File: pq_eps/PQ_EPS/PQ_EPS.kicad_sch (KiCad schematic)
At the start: 89 parts, among them IC1 DS2782E+, IC2 ISL9120IRTNZ, J1 CES-110-02-L-S, J2 CES-110-02-L-S, J3 CES-110-02-L-S, J4 CES-110-02-L-S, Q1 SIR424DP, U1 SPV1040TTR, U2 SPV1040TTR, U3 SPV1040TTR, U4 LTC4040EUFD#PBF

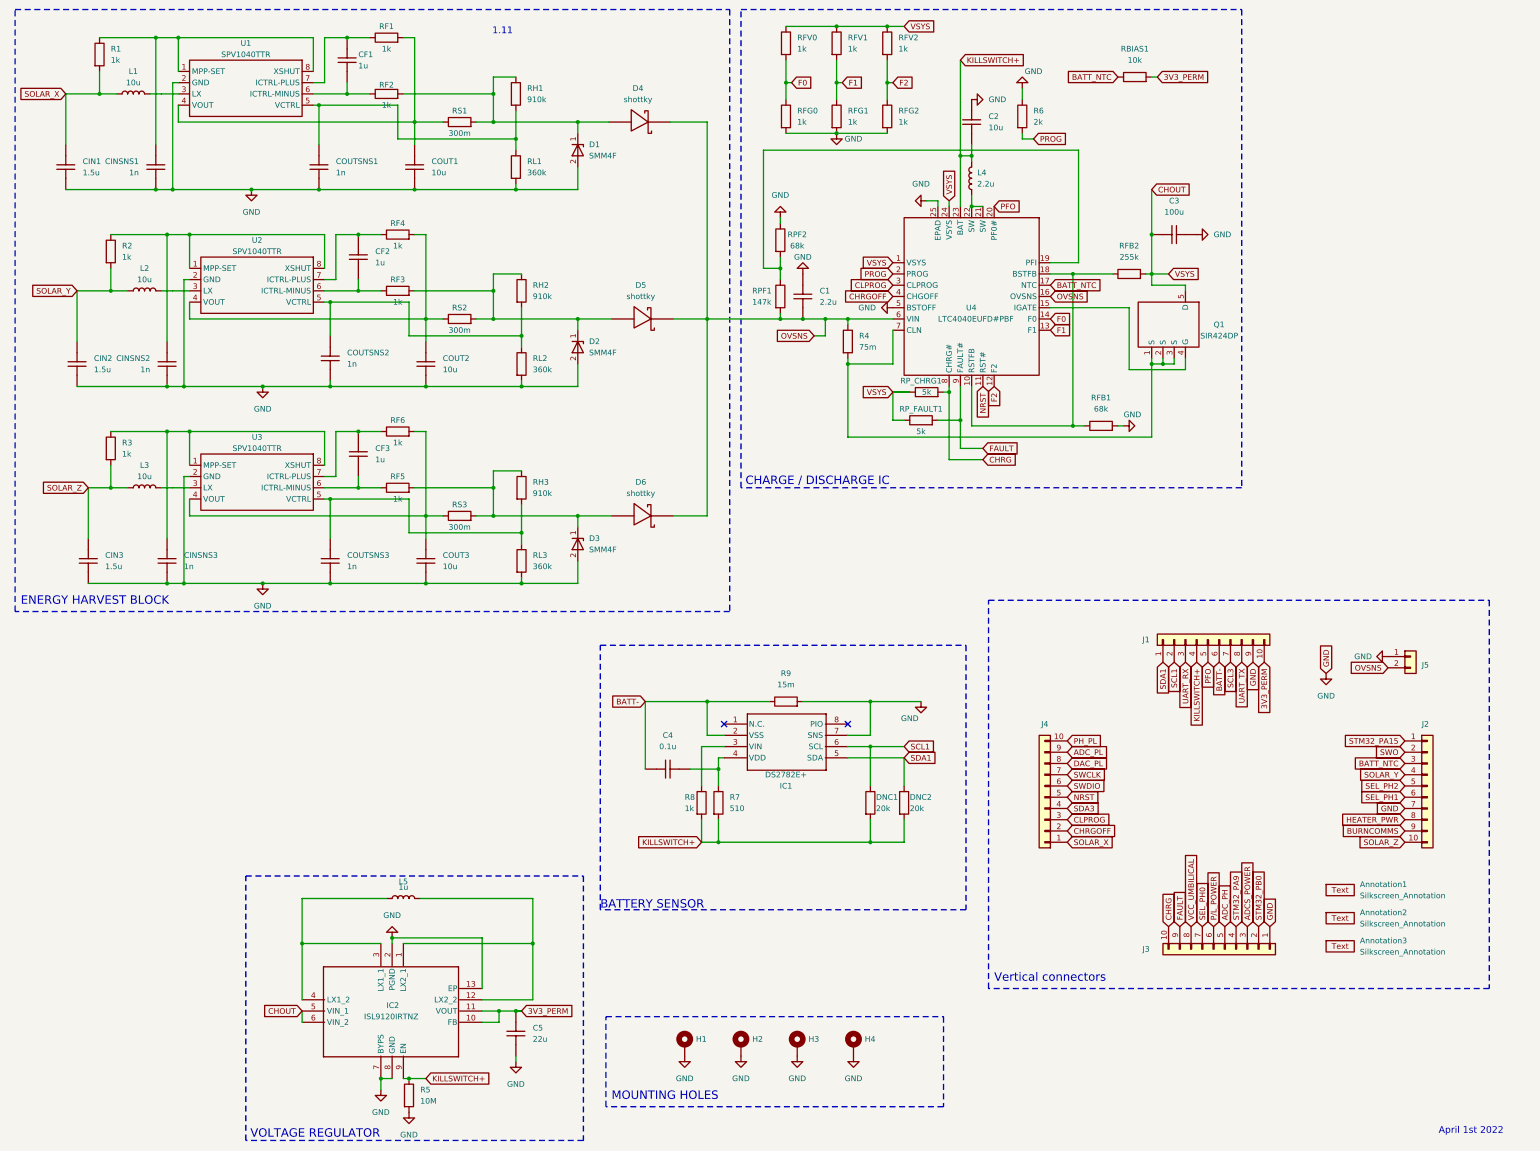
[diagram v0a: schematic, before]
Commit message: Fixed ALTIUM imported symbols and thermal relief in PCB
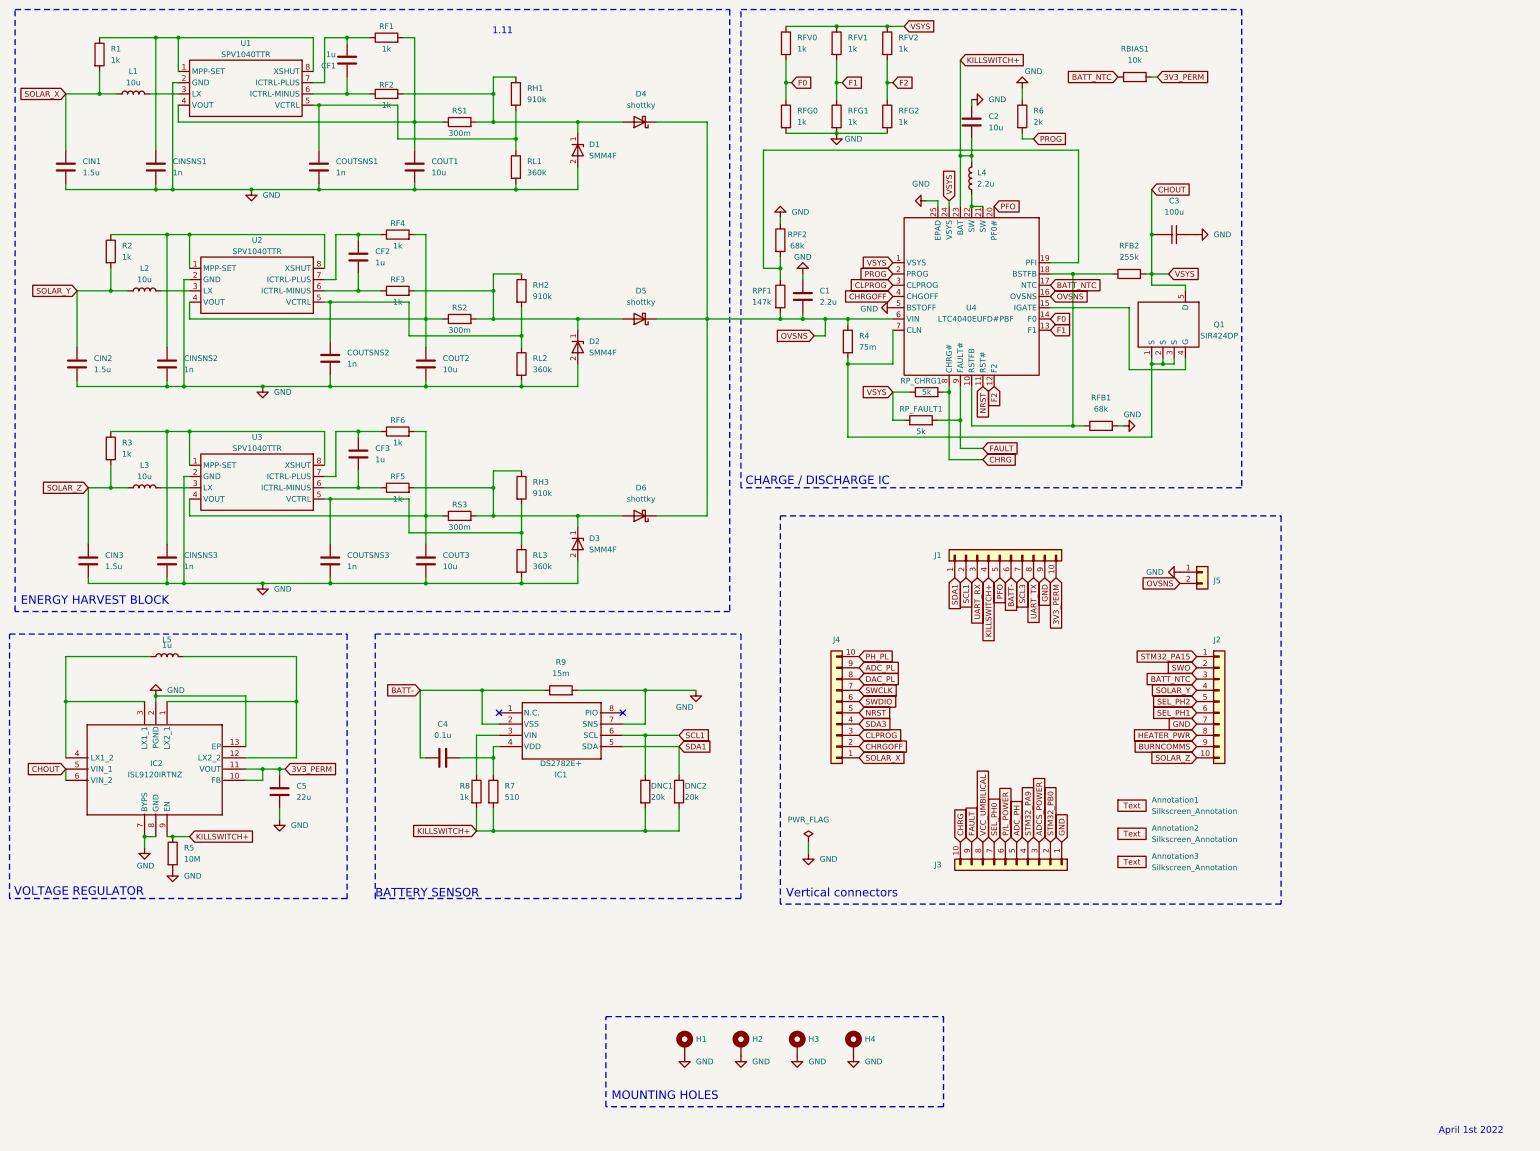
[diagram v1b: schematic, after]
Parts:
- C1: symbol PCB-EPS-altium-import:1_2.2u -> Device:C
- C2, COUT1, COUT2, COUT3: symbol PCB-EPS-altium-import:1_10u -> Device:C
- C4: symbol PCB-EPS-altium-import:2_0.1u -> Device:C
- C5: symbol PCB-EPS-altium-import:1_22u -> Device:C
- CF1, CF2, CF3: symbol PCB-EPS-altium-import:1_1u -> Device:C
- CIN1, CIN2, CIN3: symbol PCB-EPS-altium-import:1_1.5u -> Device:C
- CINSNS1, CINSNS2, CINSNS3, COUTSNS1, COUTSNS2, COUTSNS3: symbol PCB-EPS-altium-import:1_1n -> Device:C
- D4, D5, D6: symbol -nsl_passive:RBS1LAM40ATR_Schottky -> Device:D_Schottky
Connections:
- net GND: now also C1.1; no longer C1.2
- net OVSNS: now also C1.2; no longer C1.1
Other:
- moved on the sheet: Annotation1, Annotation2, Annotation3, DNC1, DNC2, IC1, IC2, J1, J2, J3, J4, J5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
